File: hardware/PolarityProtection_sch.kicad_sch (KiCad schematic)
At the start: 19 parts, among them IC1 LM74502HDDFR, Q1 NVMFWS1D7N04XMT1G, Q4 NVMFWS1D7N04XMT1G

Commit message: Bom and Final Layout
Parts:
- C1: P/N UMK107BJ105KA-T -> MLASU168SB5105KTNA01
- C4: P/N HMK107B7104KA-T -> MLASH168SB7104KTNA01
- C5: P/N MSASU168SB7224KTNB25 -> MSASU168SB7224KTNB25
- C7: value 10u -> 10uF
- C8: value 0.1u -> 0.1uF; P/N HMK107B7104KA-T -> MLASH168SB7104KTNA01
- C9: value 1u -> 1uF; P/N HMK107B7104KA-T -> MLASU168SB5105KTNA01
- D1: P/N (none) -> SMAF4758A-TP
- R1: P/N CRCW060310K0FKEI -> CRCW060310K0FKEI

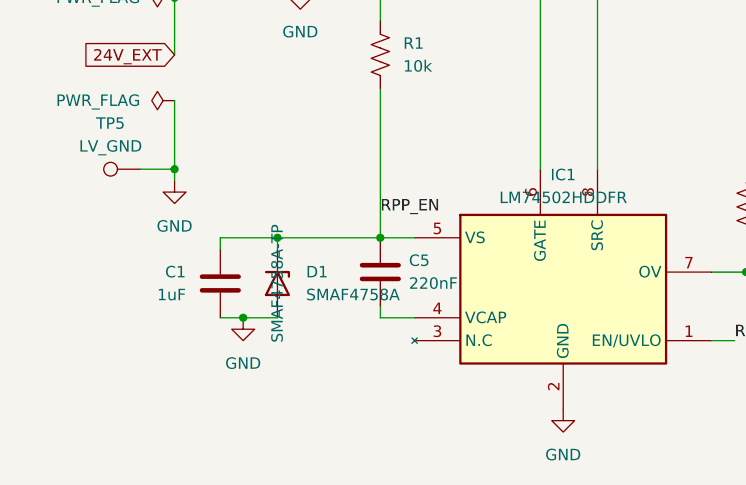
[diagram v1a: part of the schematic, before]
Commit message: add JLCPCB assembly files
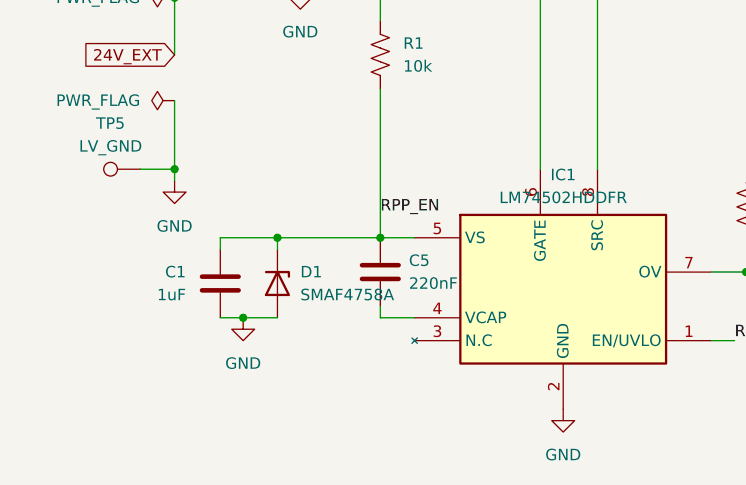
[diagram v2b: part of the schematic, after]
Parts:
- C1, C9: LCSC P/N (none) -> C15849
- C4, C8: LCSC P/N (none) -> C14663
- C5: LCSC P/N (none) -> C344195
- C6, C7: footprint Capacitor_SMD:C_0603_1608Metric -> Capacitor_SMD:C_0805_2012Metric_Pad1.18x1.45mm_HandSolder; LCSC P/N (none) -> C440198
- IC1: LCSC P/N (none) -> C5219202
- LVPWR1: LCSC P/N (none) -> C7371904
- Q1, Q4: LCSC P/N (none) -> C133142; now in the parts list
- R1: LCSC P/N (none) -> C25804
- R2: LCSC P/N (none) -> C25811
- R6: LCSC P/N (none) -> C3016444
- R7: LCSC P/N (none) -> C2907165
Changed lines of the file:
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@@
 		(unit 1)
 		(exclude_from_sim no)
-		(in_bom no)
+		(in_bom yes)
 		(on_board yes)
 		(dnp no)
@@
 		(property "P/N" "NVMFWS1D7N04XMT1G"
 			(at 135.255 88.265 0)
+			(effects
+				(font
+					(size 1.27 1.27)
+				)
+				(hide yes)
+			)
+		)
+		(property "LCSC P/N" "C133142"
+			(at 135.255 88.265 90)
 			(effects
 				(font
@@
 			)
 		)
+		(property "LCSC P/N" "C15849"
+			(at 74.93 124.46 0)
+			(effects
+				(font
+					(size 1.27 1.27)
+				)
+				(hide yes)
+			)
+		)
 		(pin "2"
 		)
@@
 			)
 		)
+		(property "LCSC P/N" "C344195"
+			(at 92.71 123.19 0)
+			(effects
+				(font
+					(size 1.27 1.27)
+				)
+				(hide yes)
+			)
+		)
 		(pin "2"
 		)
@@
 			)
 		)
+		(property "LCSC P/N" "C25804"
+			(at 92.71 99.06 0)
+			(effects
+				(font
+					(size 1.27 1.27)
+				)
+				(hide yes)
+			)
+		)
 		(pin "1"
 		)
@@
 		(unit 1)
 		(exclude_from_sim no)
-		(in_bom no)
+		(in_bom yes)
 		(on_board yes)
 		(dnp no)
@@
 			)
 		)
+		(property "LCSC P/N" "C133142"
+			(at 94.615 88.265 90)
+			(effects
+				(font
+					(size 1.27 1.27)
+				)
+				(hide yes)
+			)
+		)
 		(pin "8"
 		)
@@
 			)
 		)
+		(property "LCSC P/N" "C15849"
+			(at 248.92 95.25 0)
+			(effects
+				(font
+					(size 1.27 1.27)
+				)
+				(hide yes)
+			)
+		)
 		(pin "1"
 		)
@@
 			)
 		)
+		(property "LCSC P/N" "C14663"
+			(at 83.82 87.63 0)
+			(effects
+				(font
+					(size 1.27 1.27)
+				)
+				(hide yes)
+			)
+		)
 		(pin "1"
 		)
@@
 			)
 		)
+		(property "LCSC P/N" ""
+			(at 157.48 77.47 0)
+			(effects
+				(font
+					(size 1.27 1.27)
+				)
+				(hide yes)
+			)
+		)
 		(pin "1"
 		)
@@
 			)
 		)
+		(property "LCSC P/N" "C5219202"
+			(at 96.52 119.38 0)
+			(effects
+				(font
+					(size 1.27 1.27)
+				)
+				(hide yes)
+			)
+		)
 		(pin "1"
 		)
@@
 			)
 		)
+		(property "LCSC P/N" ""
+			(at 77.47 83.82 90)
+			(effects
+				(font
+					(size 1.27 1.27)
+				)
+				(hide yes)
+			)
+		)
 		(pin "1"
 		)
@@
 			)
 		)
+		(property "LCSC P/N" "C2907165"
+			(at 212.09 90.17 0)
+			(effects
+				(font
+					(size 1.27 1.27)
+				)
+				(hide yes)
+			)
+		)
 		(pin "1"
 		)
@@
 			)
 		)
-		(property "Footprint" "Capacitor_SMD:C_0603_1608Metric"
+		(property "Footprint" "Capacitor_SMD:C_0805_2012Metric_Pad1.18x1.45mm_HandSolder"
 			(at 148.2852 93.98 0)
 			(effects
@@
 			)
 		)
+		(property "LCSC P/N" "C440198"
+			(at 147.32 90.17 0)
+			(effects
+				(font
+					(size 1.27 1.27)
+				)
+				(hide yes)
+			)
+		)
 		(pin "2"
 		)
@@
 			)
 		)
+		(property "LCSC P/N" ""
+			(at 66.04 111.76 90)
+			(effects
+				(font
+					(size 1.27 1.27)
+				)
+				(hide yes)
+			)
+		)
 		(pin "1"
 		)
@@
 			)
 		)
+		(property "LCSC P/N" "C14663"
+			(at 238.76 95.25 0)
+			(effects
+				(font
+					(size 1.27 1.27)
+				)
+				(hide yes)
+			)
+		)
 		(pin "1"
 		)
@@
 			)
 		)
+		(property "LCSC P/N" "C3016444"
+			(at 142.24 123.19 90)
+			(effects
+				(font
+					(size 1.27 1.27)
+				)
+				(hide yes)
+			)
+		)
 		(pin "1"
 		)
@@
 		(fields_autoplaced yes)
 		(property "Reference" "D1"
-			(at 84.455 123.1899 90)
+			(at 83.82 123.1899 90)
 			(effects
 				(font
@@
 		)
 		(property "Value" "SMAF4758A"
-			(at 84.455 125.7299 90)
+			(at 83.82 125.7299 90)
 			(effects
 				(font
@@
 					(size 1.27 1.27)
 				)
+				(hide yes)
+			)
+		)
+		(property "LCSC P/N" ""
+			(at 81.28 124.46 90)
+			(effects
+				(font
+					(size 1.27 1.27)
+				)
+				(hide yes)
 			)
 		)
@@
 			)
 		)
-		(property "Footprint" "Capacitor_SMD:C_0603_1608Metric"
+		(property "Footprint" "Capacitor_SMD:C_0805_2012Metric_Pad1.18x1.45mm_HandSolder"
 			(at 227.0252 99.06 0)
 			(effects
@@
 			)
 		)
+		(property "LCSC P/N" "C440198"
+			(at 226.06 95.25 0)
+			(effects
+				(font
+					(size 1.27 1.27)
+				)
+				(hide yes)
+			)
+		)
 		(pin "1"
 		)
@@
 			)
 		)
+		(property "LCSC P/N" "C25811"
+			(at 133.35 115.57 0)
+			(effects
+				(font
+					(size 1.27 1.27)
+				)
+				(hide yes)
+			)
+		)
 		(pin "1"
 		)
@@
 			(effects
 				(font
+					(size 1.27 1.27)
+				)
+				(hide yes)
+			)
+		)
+		(property "LCSC P/N" "C7371904"
+			(at 212.09 99.06 90)
+			(effects
+				(font
